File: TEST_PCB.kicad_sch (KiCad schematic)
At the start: 66 parts, among them J101 Conn_01x03_Pin, J102 Conn_01x05_Socket, J103 Conn_01x02_Socket, J104 Conn_01x04_Socket, J105 Conn_01x03_Pin, J106 Conn_01x02_Socket, J107 Conn_01x04_Socket, J108 Conn_01x02_Socket, J109 Conn_01x02_Socket, J110 Conn_01x03_Pin, J111 Conn_01x02_Socket, J112 Conn_01x02_Socket, J113 Conn_01x02_Socket, J114 Conn_01x02_Socket, J115 Conn_01x02_Socket, J116 Conn_01x02_Pin, J117 Conn_01x02_Socket, J118 Conn_01x03_Pin, J119 Conn_01x02_Socket, J120 Conn_01x02_Socket, J121 Conn_01x02_Socket, J122 Conn_01x02_Socket, J123 Conn_01x02_Socket, J124 Conn_01x02_Socket, J125 Conn_01x02_Socket, J126 Conn_01x02_Pin, J127 Conn_01x02_Pin, J128 Conn_01x02_Pin, J129 Conn_01x02_Pin, J130 Conn_01x02_Pin, J131 Conn_01x02_Pin, J132 Conn_01x03_Socket, J133 Conn_01x03_Socket, J134 Conn_01x02_Pin, J135 Conn_01x02_Pin, J136 Conn_01x02_Pin, J137 Conn_01x05_Socket, J138 Conn_01x02_Socket, J139 Conn_01x02_Socket, J140 Conn_01x02_Socket, J141 Conn_01x02_Socket, J142 Conn_01x02_Socket, Q101 IRLML5103, U101 LP38690SDX-3.3/NOPB

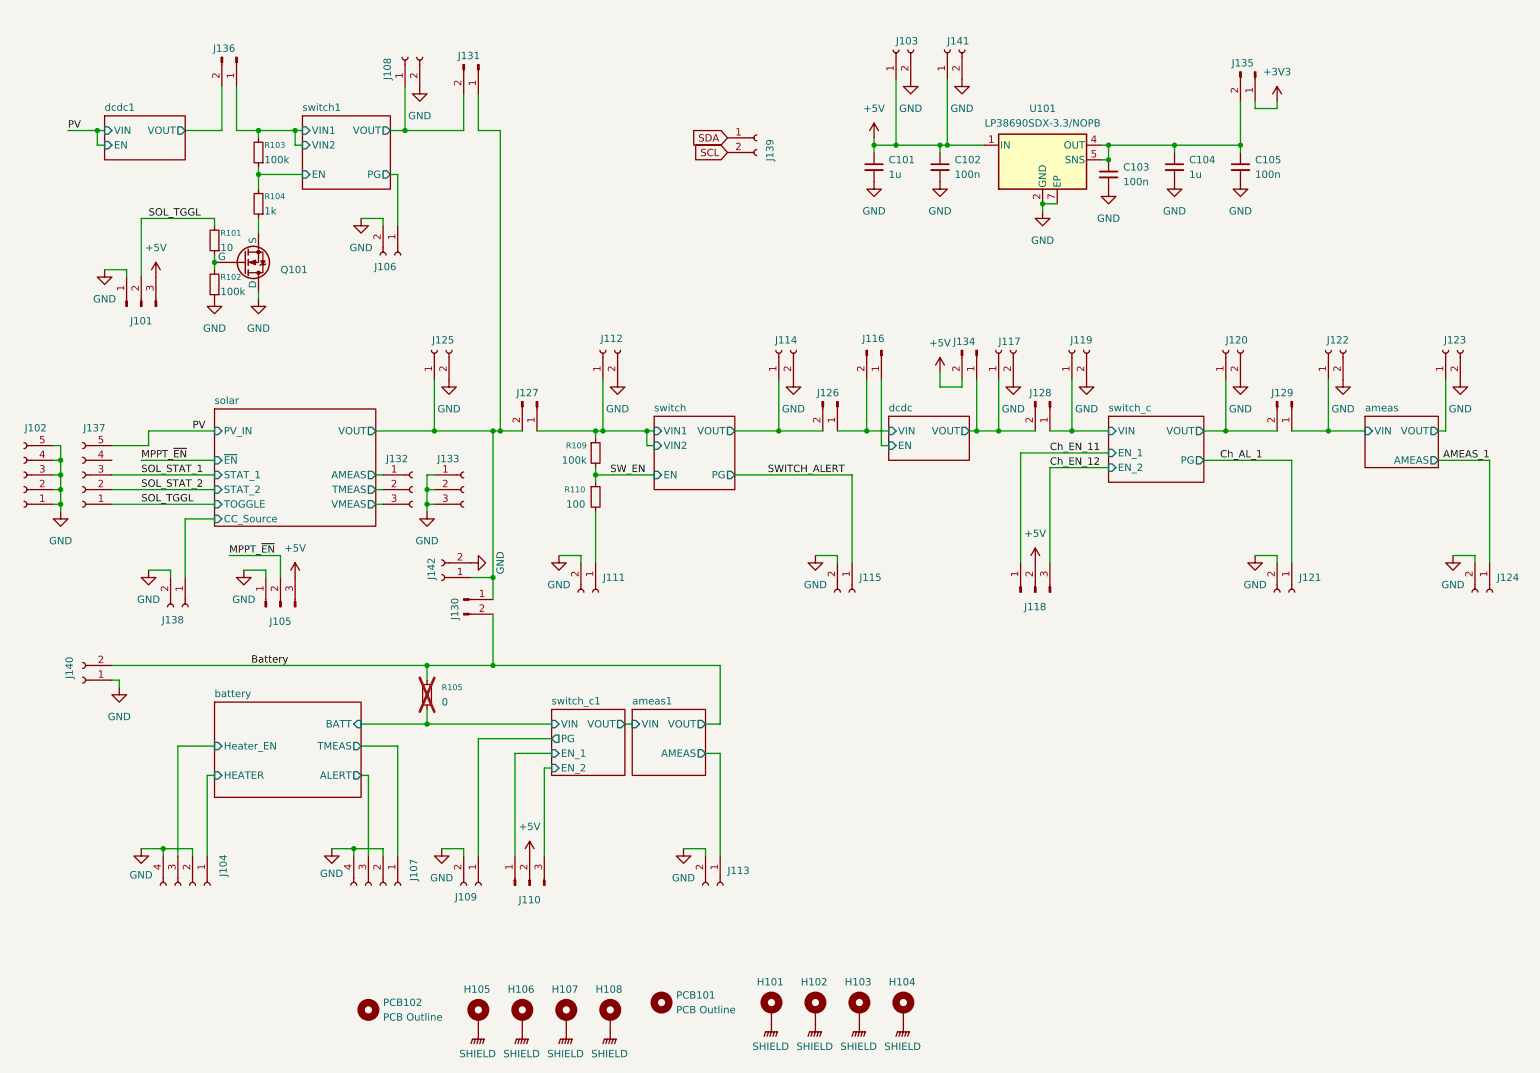
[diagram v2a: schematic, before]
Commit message: added universal switch, added simples current source, reworked test schematic and pcb
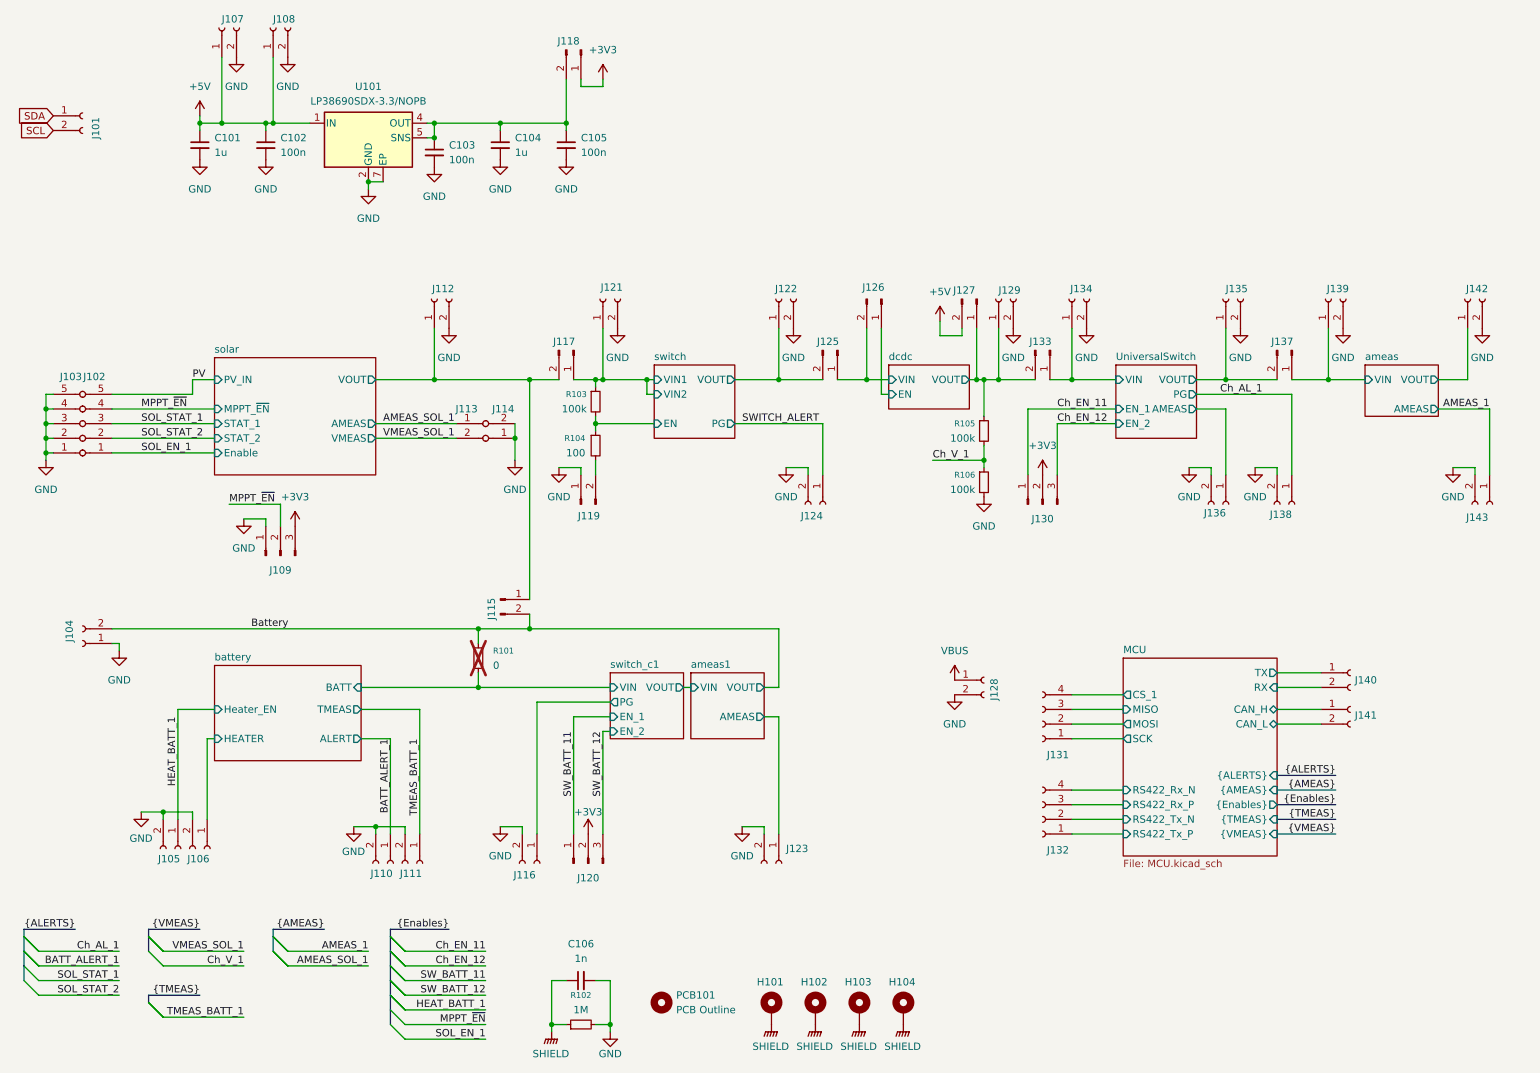
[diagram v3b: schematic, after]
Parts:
- removed H105, H106, H107, H108: MountingHole, MountingHole:MountingHole_3.2mm_M3_Pad_TopBottom, symbol Mechanical:MountingHole_Pad
- removed J101: Conn_01x03_Pin, Connector_PinHeader_2.54mm:PinHeader_1x03_P2.54mm_Vertical, symbol Connector:Conn_01x03_Pin
- removed J104, J107: Conn_01x04_Socket, Connector_PinSocket_2.54mm:PinSocket_1x04_P2.54mm_Vertical, symbol Connector:Conn_01x04_Socket
- removed J108, J138, J142: Conn_01x02_Socket, Connector_PinSocket_2.54mm:PinSocket_1x02_P2.54mm_Vertical, symbol Connector:Conn_01x02_Socket
- removed J131, J136: Conn_01x02_Pin, Connector_PinHeader_2.54mm:PinHeader_1x02_P2.54mm_Vertical, symbol Connector:Conn_01x02_Pin
- removed J132, J133: Conn_01x03_Socket, Connector_PinSocket_2.54mm:PinSocket_1x03_P2.54mm_Vertical, symbol Connector:Conn_01x03_Socket
- removed PCB102: PCB Outline, Outlines:SPACEMANIC_V1c, symbol Mechanical:MountingHole
- removed Q101: IRLML5103, Package_TO_SOT_SMD:SOT-23-3, symbol Simulation_SPICE:NMOS
- removed R101: 10, Resistor_SMD:R_0603_1608Metric_Pad0.98x0.95mm_HandSolder, symbol Device:R_Small
- removed R103: 100k, Resistor_SMD:R_0603_1608Metric_Pad0.98x0.95mm_HandSolder, symbol Device:R_Small
- removed R104: 1k, Resistor_SMD:R_0603_1608Metric_Pad0.98x0.95mm_HandSolder, symbol Device:R_Small
- added C106: 1n, Capacitor_SMD:C_0805_2012Metric_Pad1.18x1.45mm_HandSolder, symbol Device:C_Small
- added J105, J110, J113, J114, J128, J136, J140, J141: Conn_01x02_Socket, Connector_PinSocket_2.54mm:PinSocket_1x02_P2.54mm_Vertical, symbol Connector:Conn_01x02_Socket
- added J119: Conn_01x02_Pin, Connector_PinHeader_2.54mm:PinHeader_1x02_P2.54mm_Vertical, symbol Connector:Conn_01x02_Pin
- added J131, J132: Conn_01x04_Socket, Connector_PinSocket_2.54mm:PinSocket_1x04_P2.54mm_Vertical, symbol Connector:Conn_01x04_Socket
- added R105, R106: 100k, Resistor_SMD:R_0603_1608Metric_Pad0.98x0.95mm_HandSolder, symbol Device:R_Small
- R102: value 100k -> 1M
- renumbered J139 to J101, J137 to J102, J102 to J103, J140 to J104, J103 to J107, J141 to J108, J105 to J109, J125 to J112, J130 to J115, J109 to J116, J127 to J117, J135 to J118, J110 to J120, J112 to J121, J114 to J122, J113 to J123, J115 to J124, J126 to J125, J116 to J126, J134 to J127, J117 to J129, J118 to J130, J128 to J133, J119 to J134, J120 to J135, J129 to J137, J121 to J138, J122 to J139, J123 to J142, J124 to J143, R105 to R101, R109 to R103, R110 to R104
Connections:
- net switch1/PG is gone; now on net battery/HEATER: J106.1 (Pin_1)
- net +3V3: now also J109.3 (Pin_3), J120.2 (Pin_2), J130.2 (Pin_2)
- net +5V: no longer J109.3 (Pin_3), J120.2 (Pin_2), J130.2 (Pin_2)
- net GND: now also R102.2, C106.2, J105.2 (Pin_2), J110.2 (Pin_2), J114.1 (Pin_1), J114.2 (Pin_2), J119.1 (Pin_1), J128.2 (Pin_2), J136.2 (Pin_2), R106.2; no longer R102.1
- net MPPT_~{EN}: now also J102.4 (Pin_4)
- net SHIELD: now also R102.1, C106.1
- net dcdc/VOUT: now also R105.1
- net at R104.2: now also J119.2 (Pin_2); no longer J111.1 (Pin_1)
- net SOL_TGGL renamed SOL_EN_1
- net SW_EN renamed switch/EN
- net switch_c/VIN renamed UniversalSwitch/VIN
- net switch_c/VOUT renamed UniversalSwitch/VOUT
- net switch_c1/EN_1 renamed SW_BATT_11
- net switch_c1/EN_2 renamed SW_BATT_12
- new net AMEAS_SOL_1: J113.1 (Pin_1)
- new net BATT_ALERT_1: J110.1 (Pin_1)
- new net Ch_V_1: R105.2, R106.1
- new net HEAT_BATT_1: J105.1 (Pin_1)
- new net MCU/CAN_H: J141.1 (Pin_1)
- new net MCU/CAN_L: J141.2 (Pin_2)
- new net MCU/CS_1: J131.4 (Pin_4)
- new net MCU/MISO: J131.3 (Pin_3)
- new net MCU/MOSI: J131.2 (Pin_2)
- new net MCU/RS422_Rx_N: J132.4 (Pin_4)
- new net MCU/RS422_Rx_P: J132.3 (Pin_3)
- new net MCU/RS422_Tx_N: J132.2 (Pin_2)
- new net MCU/RS422_Tx_P: J132.1 (Pin_1)
- new net MCU/RX: J140.2 (Pin_2)
- new net MCU/SCK: J131.1 (Pin_1)
- new net MCU/TX: J140.1 (Pin_1)
- new net TMEAS_BATT_1: J111.1 (Pin_1)
- new net UniversalSwitch/AMEAS: J136.1 (Pin_1)
- new net VBUS: J128.1 (Pin_1)
- new net VMEAS_SOL_1: J113.2 (Pin_2)
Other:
- removed sheet dcdc1
- removed sheet switch1
- removed sheet switch_c
- added sheet MCU (MCU.kicad_sch)
- added sheet UniversalSwitch (UniversalSwitch.kicad_sch)
- sheet battery: file Battery_Cell_Input.kicad_sch -> EPS_BATTERY_PACK/EPS_BATTERY_PACK.kicad_sch
- sheet solar ports: added Enable, MPPT_~{EN}; removed CC_Source, TMEAS, TOGGLE, ~{EN}
- moved on the sheet: C101, C102, C103, C104, C105, J101, J102, J103, J104, J107, J108, J109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

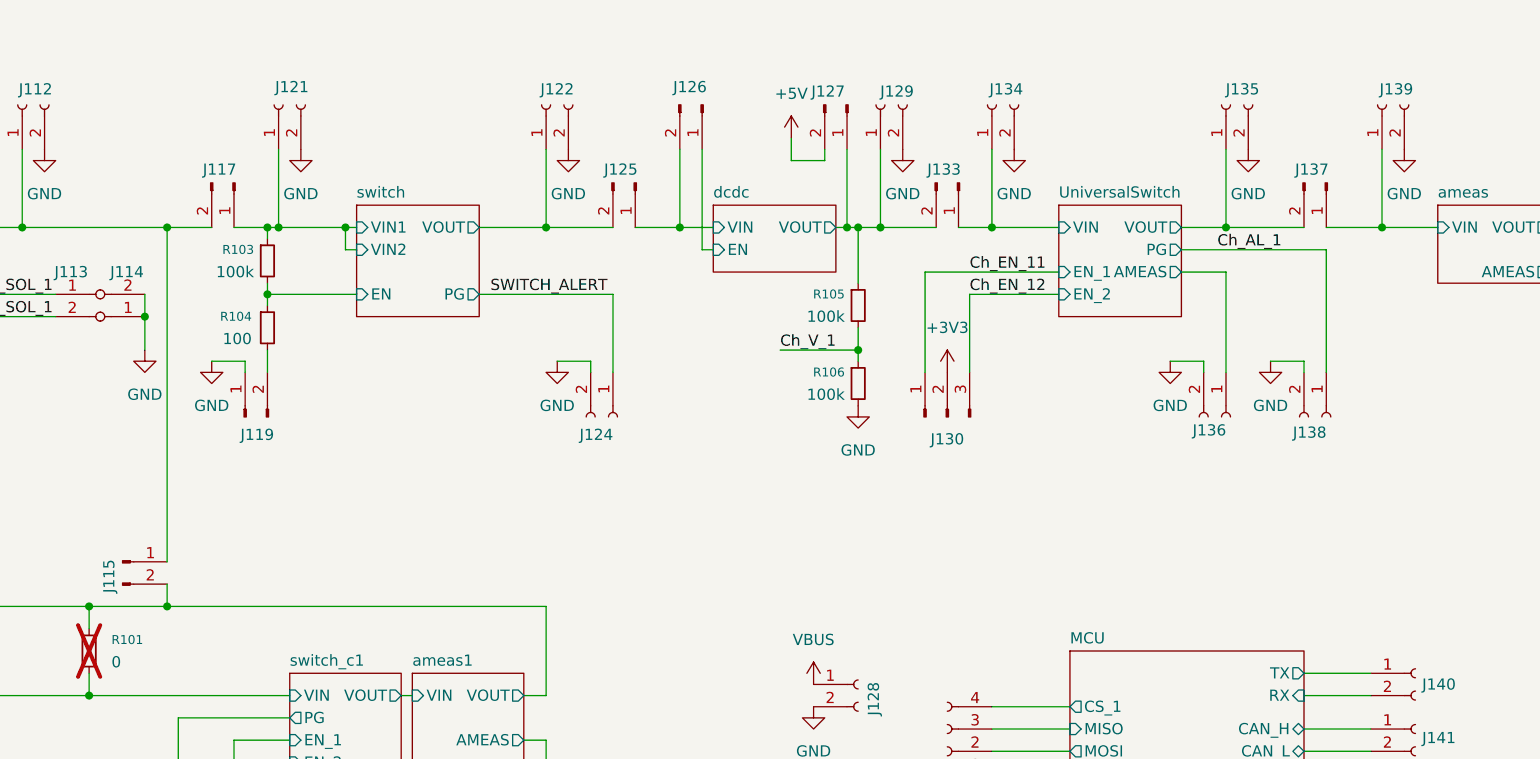
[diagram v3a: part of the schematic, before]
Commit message: specified inductors
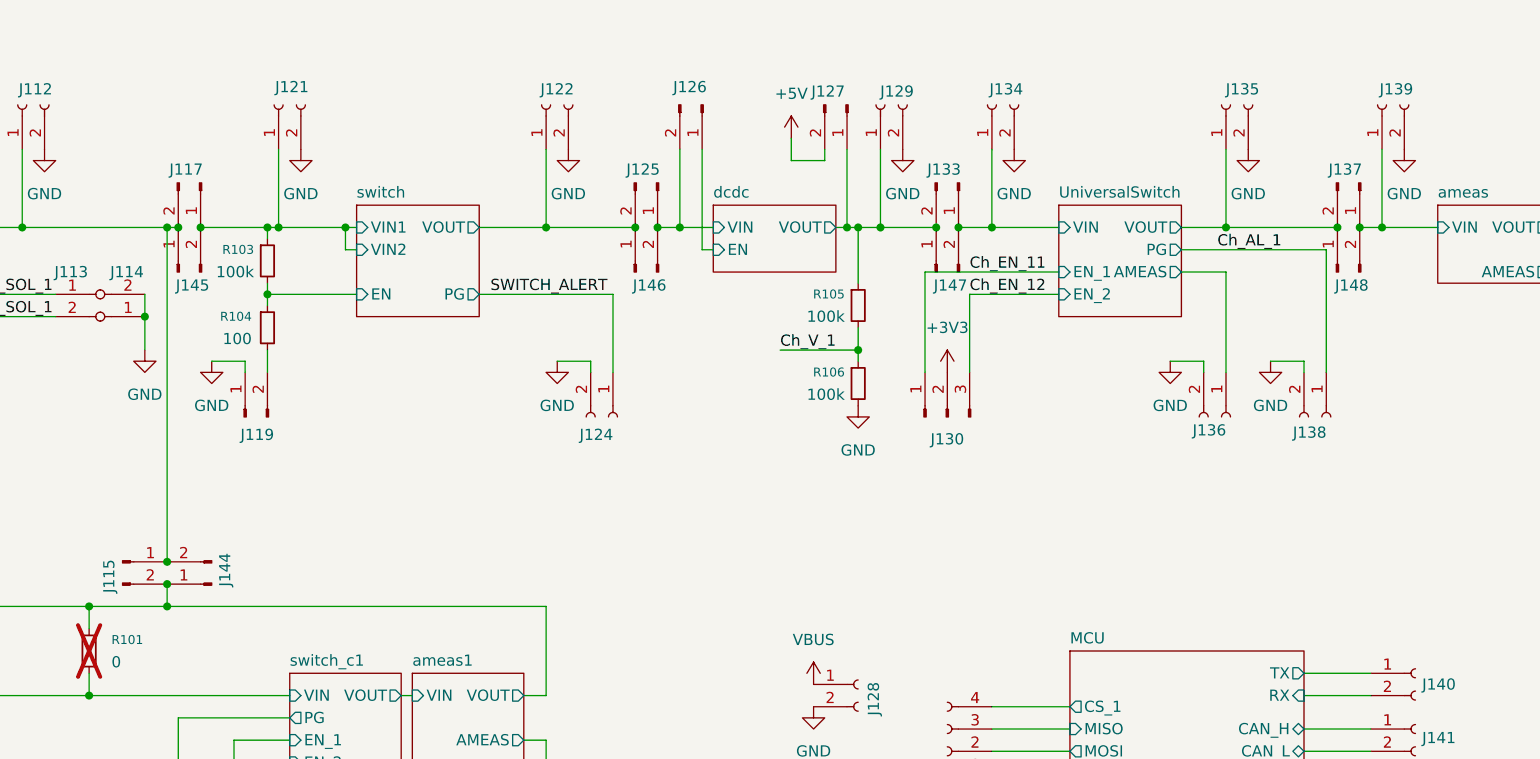
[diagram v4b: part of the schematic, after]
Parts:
- added J144, J145, J146, J147, J148: Conn_01x02_Pin, Connector_PinHeader_2.54mm:PinHeader_1x02_P2.54mm_Vertical, symbol Connector:Conn_01x02_Pin
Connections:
- net Battery: now also J144.1 (Pin_1)
- net UniversalSwitch/VIN: now also J147.2 (Pin_2)
- net UniversalSwitch/VOUT: now also J148.1 (Pin_1)
- net ameas/VIN: now also J148.2 (Pin_2)
- net dcdc/VIN: now also J146.2 (Pin_2)
- net dcdc/VOUT: now also J147.1 (Pin_1)
- net solar/VOUT: now also J144.2 (Pin_2), J145.1 (Pin_1)
- net switch/VIN1: now also J145.2 (Pin_2)
- net switch/VOUT: now also J146.1 (Pin_1)
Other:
- moved on the sheet: J117, J125, J137
